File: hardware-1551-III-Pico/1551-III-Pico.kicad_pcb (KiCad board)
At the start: 2 copper layers, 100 x 100 mm, 48 parts, among them J1 DC IN, J3 TCBM, J4 Mini-DIN-7, J8 Module_Panel, M1 Mounting, M2 Mounting, M3 Mounting, M4 Mounting, Q1 MMBT3904, Q2 MMBT3904, Q3 MMBT3904, Q4 MMBT3904

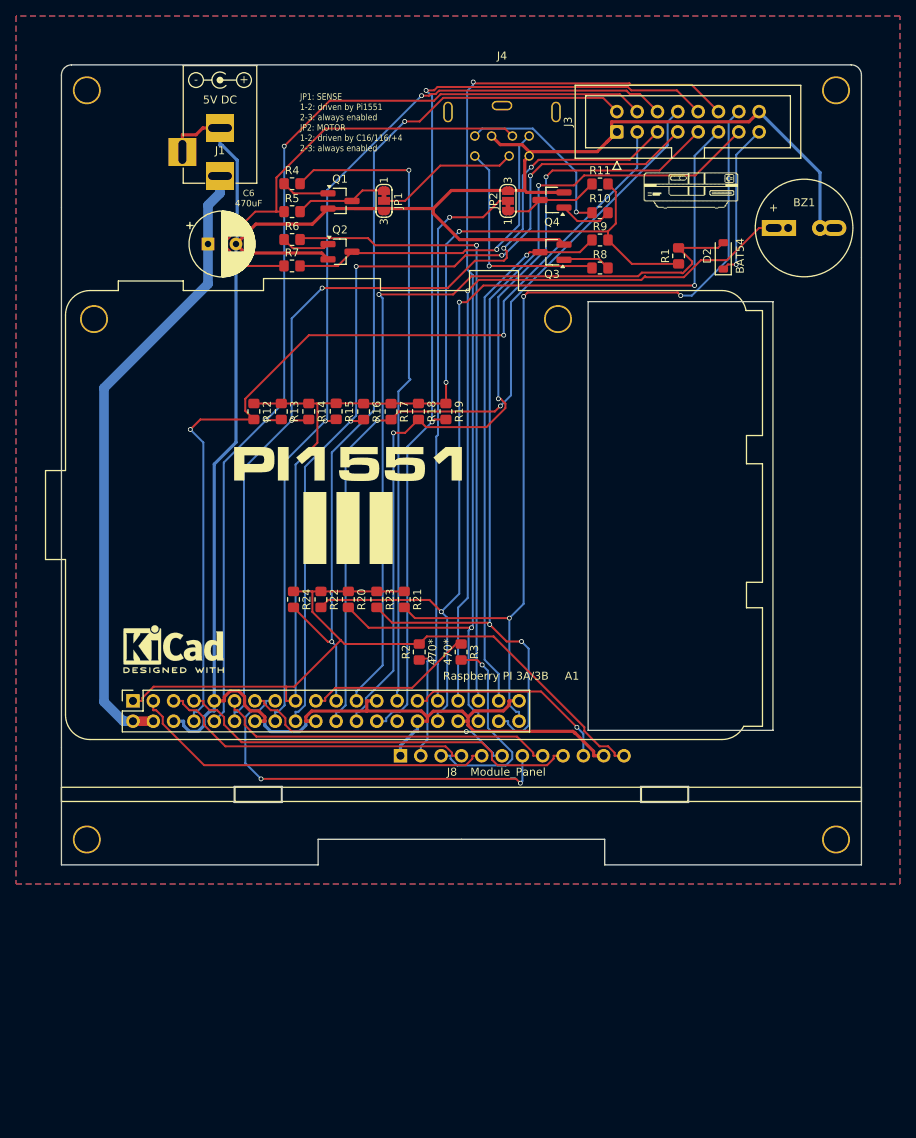
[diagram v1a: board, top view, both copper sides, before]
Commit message: mos6502 replacer integrated
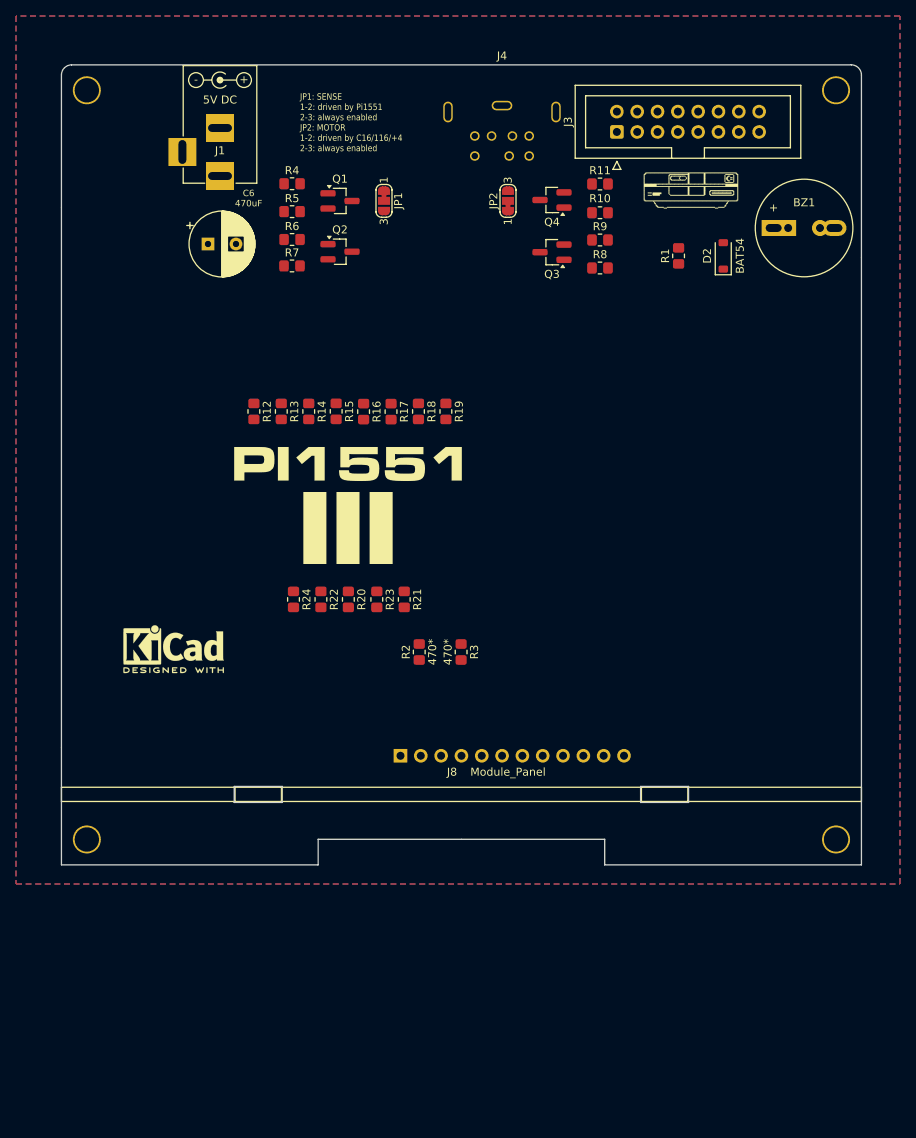
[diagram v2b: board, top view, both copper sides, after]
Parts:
- removed A1: Raspberry PI 3A/3B, RPI:Raspberry_Pi_3B_Socketed_THT_FaceDown_MountingHoles
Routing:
- net GND: track 314.0 -> 0.00 mm
- net +3.3V: track 217.4 -> 0.00 mm, vias 3 -> 0
- net /STATUS0: track 130.2 -> 0.00 mm, vias 2 -> 0
- net /DIO2: track 125.1 -> 0.00 mm, vias 2 -> 0
- net /DAV: track 121.1 -> 0.00 mm, vias 3 -> 0
- net /ACK: track 120.7 -> 0.00 mm, vias 3 -> 0
- net /DIO8: track 120.7 -> 0.00 mm, vias 2 -> 0
- net /DIO4: track 118.3 -> 0.00 mm, vias 2 -> 0
- net /DIO1: track 117.3 -> 0.00 mm, vias 2 -> 0
- net /DIO3: track 116.2 -> 0.00 mm, vias 4 -> 0
- net /STATUS1: track 115.1 -> 0.00 mm, vias 3 -> 0
- net /DIO5: track 112.9 -> 0.00 mm, vias 4 -> 0
- net /DEV: track 111.4 -> 0.00 mm, vias 2 -> 0
- net /DIO7: track 107.5 -> 0.00 mm, vias 3 -> 0
- net /DIO6: track 102.1 -> 0.00 mm, vias 2 -> 0
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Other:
- outline, holes or cut-outs redrawn

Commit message: all the footprints from other projects
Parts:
- removed J4: Mini-DIN-7, Conn_DIN_round:Mini_DIN_round_7_canned
- SYM1: footprint BulkyMIDI-32:PWR_Specification -> pi1541:PWR_Specification

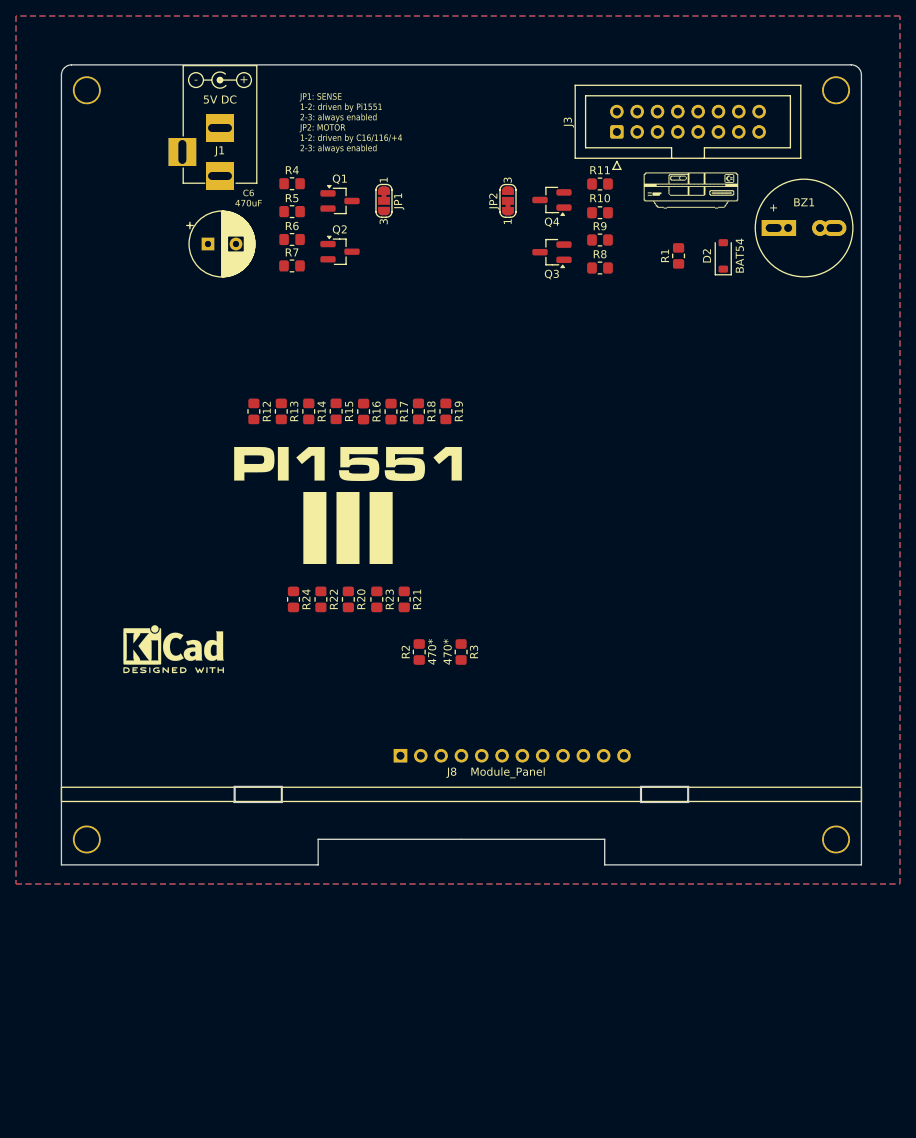
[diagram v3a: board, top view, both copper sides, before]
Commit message: part placement and routing test
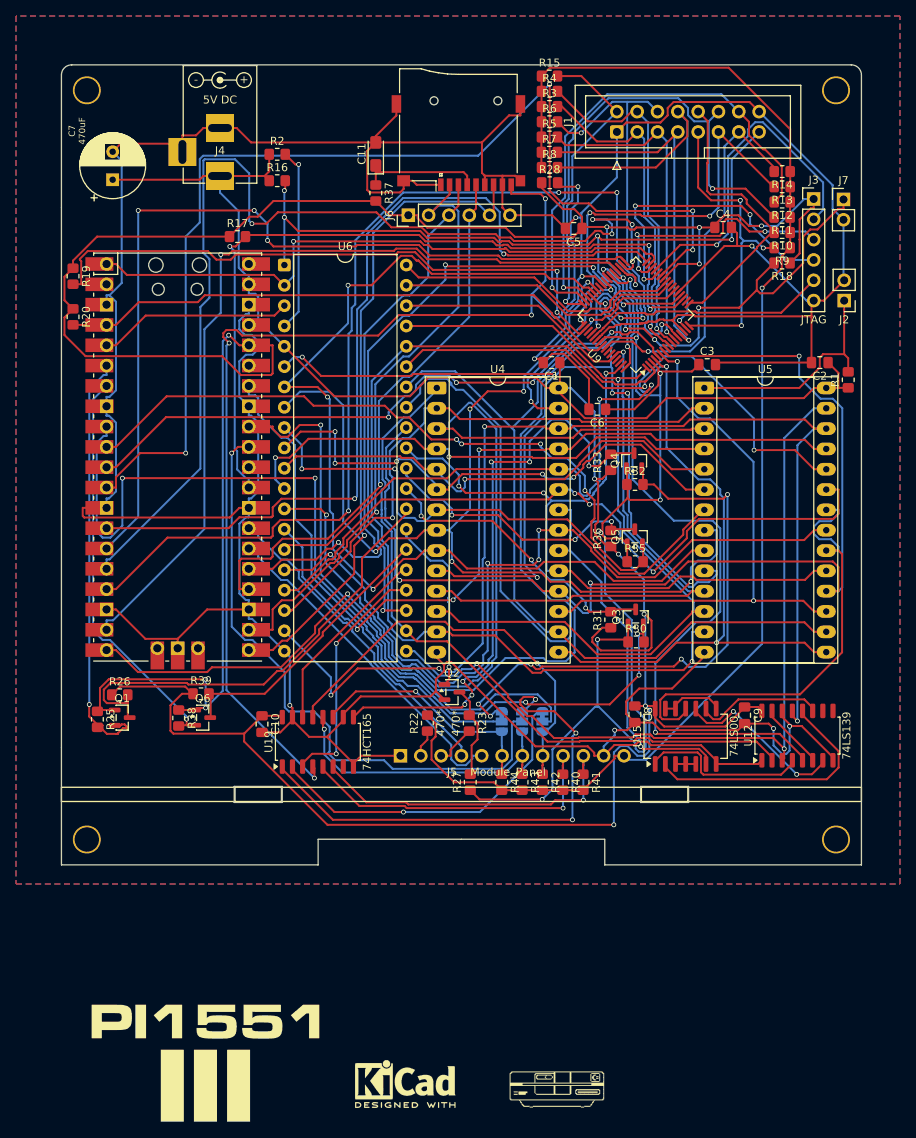
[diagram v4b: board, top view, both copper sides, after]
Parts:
- removed BZ1: Buzzer, small_buzzer:Buzzer_12x9.5RM7.6
- removed D2: BAT54, Diode_SMD:D_SOD-123
- removed the R10 at (137.5, 73.1)
- removed the R11 at (137.5, 69.5)
- removed the R4 at (99.0, 69.5)
- removed the R5 at (99.0, 73.0)
- removed the R6 at (99.0, 76.4)
- removed the R7 at (99.0, 79.7)
- removed the R8 at (137.5, 80.0)
- removed the R9 at (137.5, 76.5)
- added C1: 0.1uF, Capacitor_SMD:C_0805_2012Metric_Pad1.18x1.45mm_HandSolder, F.Cu at (131.4, 91.8)
- added C10: 0.1uF, Capacitor_SMD:C_0805_2012Metric_Pad1.18x1.45mm_HandSolder, F.Cu at (95.2, 137.0)
- added C11: 10µ, Capacitor_Tantalum_SMD:CP_EIA-3216-12_Kemet-S_HandSolder, F.Cu at (109.5, 65.7)
- added C2: 0.1uF, Capacitor_SMD:C_0805_2012Metric_Pad1.18x1.45mm_HandSolder, F.Cu at (165.0, 91.8)
- added C3: 0.1uF, Capacitor_SMD:C_0805_2012Metric_Pad1.18x1.45mm_HandSolder, F.Cu at (150.9, 92.1)
- added C4: 0.1uF, Capacitor_SMD:C_0805_2012Metric_Pad1.18x1.45mm_HandSolder, F.Cu at (152.9, 74.9)
- added C5: 0.1uF, Capacitor_SMD:C_0805_2012Metric_Pad1.18x1.45mm_HandSolder, F.Cu at (134.2, 75.1)
- added C6: 0.1uF, Capacitor_SMD:C_0805_2012Metric_Pad1.18x1.45mm_HandSolder, F.Cu at (137.2, 97.7)
- added C8: 0.1uF, Capacitor_SMD:C_0805_2012Metric_Pad1.18x1.45mm_HandSolder, F.Cu at (141.9, 135.8)
- added C9: 0.1uF, Capacitor_SMD:C_0805_2012Metric_Pad1.18x1.45mm_HandSolder, F.Cu at (155.6, 135.9)
- added J2: Conn_01x02_Pin, Connector_PinHeader_2.54mm:PinHeader_1x02_P2.54mm_Vertical, F.Cu at (168.0, 84.1)
- added J3: JTAG, Connector_PinHeader_2.54mm:PinHeader_1x06_P2.54mm_Vertical, F.Cu at (164.2, 71.4)
- added J6: SD CARD, Connector_PinHeader_2.54mm:PinHeader_1x06_P2.54mm_Vertical, F.Cu at (113.5, 73.4)
- added J7: Conn_01x02_Pin, Connector_PinHeader_2.54mm:PinHeader_1x02_P2.54mm_Vertical, F.Cu at (167.9, 71.4)
- added JP3: SolderJumper_3_Bridged12, Jumper:SolderJumper-3_P1.3mm_Bridged12_RoundedPad1.0x1.5mm_NumberLabels, B.Cu at (127.8, 136.7)
- added Q5: BSS138, Package_TO_SOT_SMD:SOT-23, F.Cu at (141.9, 113.6)
- added Q6: BSS138, Package_TO_SOT_SMD:SOT-23, F.Cu at (87.8, 136.2)
- added R16: 3.3K, Resistor_SMD:R_0805_2012Metric_Pad1.20x1.40mm_HandSolder, F.Cu at (97.2, 69.1)
- added R17: 3.3K, Resistor_SMD:R_0805_2012Metric_Pad1.20x1.40mm_HandSolder, F.Cu at (92.2, 76.1)
- added R18: 3.3K, Resistor_SMD:R_0805_2012Metric_Pad1.20x1.40mm_HandSolder, F.Cu at (160.3, 79.4)
- added R19: 3.3K, Resistor_SMD:R_0805_2012Metric_Pad1.20x1.40mm_HandSolder, F.Cu at (71.6, 81.0)
- added R2: 3.3K, Resistor_SMD:R_0805_2012Metric_Pad1.20x1.40mm_HandSolder, F.Cu at (97.2, 65.8)
- added R20: 3.3K, Resistor_SMD:R_0805_2012Metric_Pad1.20x1.40mm_HandSolder, F.Cu at (71.6, 86.1)
- added R25: 3.3K, Resistor_SMD:R_0805_2012Metric_Pad1.20x1.40mm_HandSolder, F.Cu at (74.7, 136.4)
- added R26: 3.3K, Resistor_SMD:R_0805_2012Metric_Pad1.20x1.40mm_HandSolder, F.Cu at (77.5, 133.3)
- added R27: 3.3K, Resistor_SMD:R_0805_2012Metric_Pad1.20x1.40mm_HandSolder, F.Cu at (121.3, 144.3)
- added R28: 3.3K, Resistor_SMD:R_0805_2012Metric_Pad1.20x1.40mm_HandSolder, F.Cu at (131.2, 69.3)
- added R30: 3.3K, Resistor_SMD:R_0805_2012Metric_Pad1.20x1.40mm_HandSolder, F.Cu at (142.0, 126.7)
- added R31: 3.3K, Resistor_SMD:R_0805_2012Metric_Pad1.20x1.40mm_HandSolder, F.Cu at (138.8, 124.0)
- added R32: 3.3K, Resistor_SMD:R_0805_2012Metric_Pad1.20x1.40mm_HandSolder, F.Cu at (141.9, 107.1)
- added R33: 3.3K, Resistor_SMD:R_0805_2012Metric_Pad1.20x1.40mm_HandSolder, F.Cu at (138.8, 104.3)
- added R35: 3.3K, Resistor_SMD:R_0805_2012Metric_Pad1.20x1.40mm_HandSolder, F.Cu at (141.9, 116.7)
- added R36: 3.3K, Resistor_SMD:R_0805_2012Metric_Pad1.20x1.40mm_HandSolder, F.Cu at (138.8, 113.8)
- added R37: 2.2R, Resistor_SMD:R_0805_2012Metric_Pad1.20x1.40mm_HandSolder, F.Cu at (109.5, 70.6)
- added R38: 3.3K, Resistor_SMD:R_0805_2012Metric_Pad1.20x1.40mm_HandSolder, F.Cu at (84.8, 136.3)
- added R39: 3.3K, Resistor_SMD:R_0805_2012Metric_Pad1.20x1.40mm_HandSolder, F.Cu at (87.6, 133.2)
- added R40: 3.3K, Resistor_SMD:R_0805_2012Metric_Pad1.20x1.40mm_HandSolder, F.Cu at (132.8, 144.3)
- added R41: 3.3K, Resistor_SMD:R_0805_2012Metric_Pad1.20x1.40mm_HandSolder, F.Cu at (135.4, 144.3)
- added R42: 3.3K, Resistor_SMD:R_0805_2012Metric_Pad1.20x1.40mm_HandSolder, F.Cu at (130.3, 144.3)
- added R43: 3.3K, Resistor_SMD:R_0805_2012Metric_Pad1.20x1.40mm_HandSolder, F.Cu at (127.8, 144.3)
- added R44: 3.3K, Resistor_SMD:R_0805_2012Metric_Pad1.20x1.40mm_HandSolder, F.Cu at (125.2, 144.3)
- added U12: 74LS139, Package_SO:SOP-16_4.4x10.4mm_P1.27mm, F.Cu at (162.2, 138.4)
- added U15: 74LS00, Package_SO:SO-14_5.3x10.2mm_P1.27mm, F.Cu at (148.2, 138.5)
- added U19: 74HCT165, Package_SO:SOP-16_4.4x10.4mm_P1.27mm, F.Cu at (102.2, 139.2)
- added U3: Pico, RPi_Pico:RPi_Pico_SMD_TH, F.Cu at (84.7, 103.6)
- added U4: KM62256CLP, Package_DIP:DIP-28_W15.24mm_Socket_LongPads, F.Cu at (117.1, 95.0)
- added U5: 27C512, Package_DIP:DIP-28_W15.24mm_Socket_LongPads, F.Cu at (150.5, 95.0)
- added U6: 6510T, Package_DIP:DIP-40_W15.24mm, F.Cu at (98.0, 79.6)
- added U9: XC9572XL-VQ64, Package_QFP:TQFP-64_10x10mm_P0.5mm, F.Cu at (142.0, 85.9)
- added XS1: SD connector, SD2IECplug:Conn_uSDcard, F.Cu at (119.8, 59.1)
- JP1, JP2: moved to B.Cu
- Q1, Q2, Q3, Q4: value MMBT3904 -> BSS138; footprint Package_TO_SOT_SMD:SOT-23_Handsoldering -> Package_TO_SOT_SMD:SOT-23
- moved Pi1541-drive 113.6 mm to (125.7, 178.7)
- moved R13 77.4 mm to (160.3, 69.8), turned to 180 degrees
- moved R14 73.7 mm to (160.3, 67.9), turned to 180 degrees
- moved R15 72.8 mm to (131.2, 56.0), turned to 0 degrees
- moved R11 72.3 mm to (160.3, 73.7), turned to 180 degrees
- moved kibuzzard-69864AC5 72.0 mm to (88.2, 174.2)
- moved kibuzzard-69864AE8 72.0 mm to (88.2, 182.2)
- moved Q1 70.1 mm to (77.8, 136.2)
- moved R12 68.6 mm to (160.3, 71.8), turned to 180 degrees
- moved JP1 66.7 mm to (125.2, 136.7)
- moved JP2 65.2 mm to (130.3, 136.7), turned to -90 degrees
- moved REF1 61.6 mm to (113.2, 182.0)
- moved REF2 61.6 mm to (113.2, 181.7)
- moved Q2 56.8 mm to (119.0, 133.0)
- moved R3 53.1 mm to (131.2, 59.8), turned to 0 degrees
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- renumbered C6 to C7, J3 to J1, J1 to J4, J8 to J5, R19 to R10, R20 to R11, R21 to R12, R22 to R13, R23 to R14, R24 to R15, R2 to R22, R3 to R23, R12 to R3, R13 to R4, R14 to R5, R15 to R6, R16 to R7, R17 to R8, R18 to R9
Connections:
- J5 pad 4: I2C_SCL -> /I2C_SCL
- J5 pad 5: I2C_SDA -> /I2C_SDA
- J5 pad 6: SW1_ENTER -> /ROT_SW
- J5 pad 7: SW2_UP -> /ROT_CLK
- J5 pad 8: SW3_DOWN -> /ROT_DT
- JP1 pad 1: Net-(JP1-A) -> /SERIAL_DT_3V3
- JP1 pad 2: /CAS_SENSE -> /ROT_SW_PICO
- JP1 pad 3: GND -> /ROT_SW
- JP2 pad 1: Net-(JP2-A) -> /SERIAL_CLK
- JP2 pad 2: /TAP_MOTOR -> /ROT_DT_PICO
- JP2 pad 3: GND -> /ROT_DT
- Q1 pad 1: Net-(Q1-B) -> +3V3
- Q1 pad 2: GND -> /MTR_3V3
- Q1 pad 3: Net-(JP1-A) -> /MTR
- Q2 pad 1: Net-(Q2-B) -> /ACT
- Q2 pad 3: /CAS_READ -> /ACT_3V3
- Q3 pad 1: Net-(Q3-B) -> +3V3
- Q3 pad 2: GND -> /STP0_3V3
- Q3 pad 3: /TAP_WRITE -> /STP0
- Q4 pad 1: Net-(Q4-B) -> +3V3
- Q4 pad 2: GND -> /SERIAL_DT_3V3
- Q4 pad 3: Net-(JP2-A) -> /SERIAL_DT
- R1 pad 1: +3.3V -> +5V
- R1 pad 2: /~{RESET_3V3} -> Net-(J2-Pin_1)
- R23 pad 1: RPI_LED -> /ACT_3V3
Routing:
- net GND: track 0.00 -> 588.6 mm, vias 0 -> 8
- net +3V3: track 0.00 -> 411.8 mm, vias 0 -> 14
- net +5V: track 0.00 -> 320.8 mm, vias 0 -> 5
- net +3.3V: track 0.00 -> 169.2 mm, vias 0 -> 1
- net /SD_CD: track 0.00 -> 148.2 mm, vias 0 -> 5
- net /YB7: track 0.00 -> 144.2 mm, vias 0 -> 4
- net /A13: track 0.00 -> 143.9 mm, vias 0 -> 4
- net /YB1: track 0.00 -> 139.9 mm, vias 0 -> 4
- net /D6: track 0.00 -> 138.9 mm, vias 0 -> 3
- net /YB4: track 0.00 -> 133.8 mm, vias 0 -> 5
- net /A0: track 0.00 -> 133.4 mm, vias 0 -> 6
- net /A1: track 0.00 -> 129.8 mm, vias 0 -> 3
- net /A2: track 0.00 -> 127.8 mm, vias 0 -> 6
- net /D5: track 0.00 -> 124.9 mm, vias 0 -> 2
- net /YB5: track 0.00 -> 120.2 mm, vias 0 -> 4
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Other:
- board text removed: "JP1: SENSE 1-2: driven by Pi1551 2-3: always enabled JP2: MOTOR 1-2: driven by C16/116/+4 2-3: always enabled"

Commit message: project updated and routed: IRQ with pullup, correct 3V3 net, correct inputs for '139
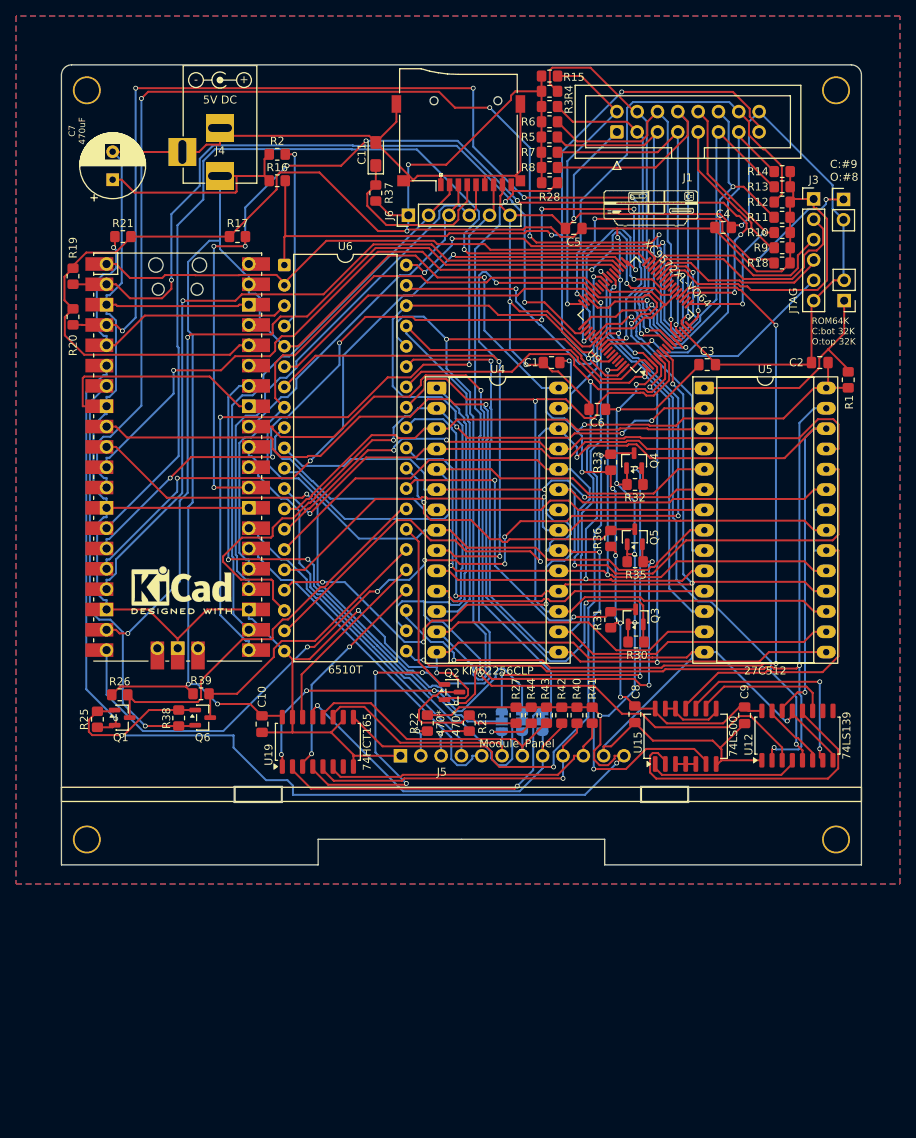
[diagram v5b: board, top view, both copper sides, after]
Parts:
- removed kibuzzard-69864AC5: G***, kibuzzard-69864AC5
- removed kibuzzard-69864AE8: G***, kibuzzard-69864AE8
- added R21: 3.3K, Resistor_SMD:R_0805_2012Metric_Pad1.20x1.40mm_HandSolder, F.Cu at (77.9, 76.1)
- moved Pi1541-drive 110.8 mm to (137.4, 68.6)
- moved REF1 67.8 mm to (85.2, 120.3)
- moved REF2 67.8 mm to (85.2, 120.0)
- moved R27 10.1 mm to (127.0, 135.9), turned to -90 degrees
- moved R44 9.14 mm to (128.9, 135.9), turned to 90 degrees
- moved R43 8.90 mm to (130.8, 135.9), turned to 90 degrees
- moved R42 8.71 mm to (132.7, 135.9), turned to 90 degrees
- moved R40 8.55 mm to (134.6, 135.9), turned to 90 degrees
- moved R41 8.44 mm to (136.5, 135.9), turned to 90 degrees
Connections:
- J5 pad 12: +3.3V -> +3V3
- R10 pad 1: +3.3V -> +3V3
- R11 pad 1: +3.3V -> +3V3
- R12 pad 1: +3.3V -> +3V3
- R13 pad 1: +3.3V -> +3V3
- R14 pad 1: +3.3V -> +3V3
- R15 pad 1: +3.3V -> +3V3
- R22 pad 2: +3.3V -> +3V3
- R3 pad 1: +3.3V -> +3V3
- R4 pad 1: +3.3V -> +3V3
- R40 pad 2: +3.3V -> +3V3
- R41 pad 2: +3.3V -> +3V3
- R42 pad 2: +3.3V -> +3V3
- R43 pad 2: +3.3V -> +3V3
- R44 pad 2: +3.3V -> +3V3
- R5 pad 1: +3.3V -> +3V3
- R6 pad 1: +3.3V -> +3V3
- R7 pad 1: +3.3V -> +3V3
- R8 pad 1: +3.3V -> +3V3
- R9 pad 1: +3.3V -> +3V3
- U12 pad 13: /A13 -> GND
- U12 pad 14: GND -> /A13
- U12 pad 2: /A15 -> /A14
- U12 pad 3: /A14 -> /A15
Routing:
- net +3.3V: track 169.2 -> 0.00 mm, vias 1 -> 0
- net /SYNC_3V3: track 70.9 -> 131.7 mm, vias 0 -> 6
- net /A7: track 116.9 -> 58.2 mm, vias 1 -> 0
- net /YB4: track 133.8 -> 88.2 mm, vias 5 -> 3
- net +3V3: track 411.8 -> 452.4 mm
- net /SD_CD: track 148.2 -> 114.1 mm, vias 5 -> 4
- net /D6: track 138.9 -> 105.8 mm
- net /BYTE_READY_3V3: track 98.2 -> 130.9 mm, vias 3 -> 8
- net /STP1_3V3: track 86.1 -> 110.5 mm
- net /R/~{W}: track 36.4 -> 59.9 mm, vias 0 -> 2
- net /A10: track 100.0 -> 76.8 mm, vias 4 -> 1
- net /BYTE_LATCHED: track 84.6 -> 107.0 mm, vias 4 -> 3
- net /YB5: track 120.2 -> 98.9 mm, vias 4 -> 1
- net /SERIAL_DT_3V3: track 71.8 -> 51.3 mm, vias 5 -> 3
- net +5V: track 320.8 -> 300.3 mm, vias 5 -> 10
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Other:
- board text added: "1551-III-Pico v1.0 Maciej Wiktowiak <ytm@elysium.pl> VIII 2026"
- board text added: "C:#9 O:#8"
- board text added: "ROM64K C:bot 32K O:top 32K"
